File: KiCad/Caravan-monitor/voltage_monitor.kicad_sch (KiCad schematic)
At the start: 2 parts, among them IC3 INA500CIDBVR

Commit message: Schematics done
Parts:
- C12: footprint Capacitor_SMD:C_0805_2012Metric_Pad1.18x1.45mm_HandSolder -> Capacitor_SMD:C_0402_1005Metric_Pad0.74x0.62mm_HandSolder
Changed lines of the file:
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@@
 			)
 		)
-		(property "Footprint" "Capacitor_SMD:C_0805_2012Metric_Pad1.18x1.45mm_HandSolder"
+		(property "Footprint" "Capacitor_SMD:C_0402_1005Metric_Pad0.74x0.62mm_HandSolder"
 			(at 157.1752 83.82 0)
 			(effects

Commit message: PCB Designed
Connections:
- net 5V renamed Vin
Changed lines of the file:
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@@
 		)
 	)
-	(hierarchical_label "5V"
+	(hierarchical_label "Vin"
 		(shape input)
 		(at 149.86 71.12 90)

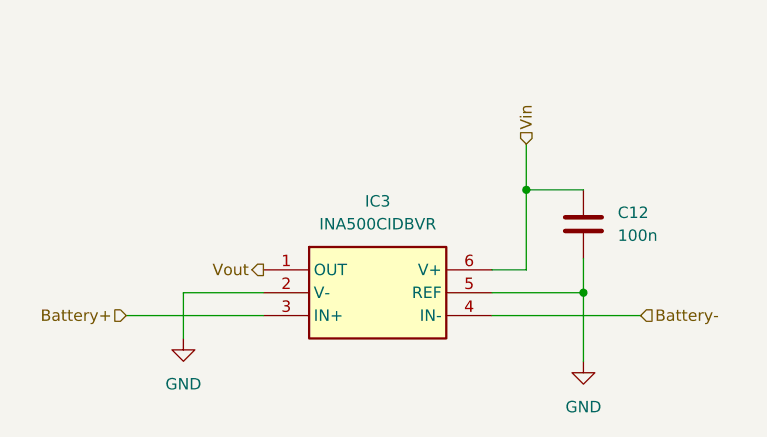
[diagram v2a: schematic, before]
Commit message: Schematic updates
Parts changed for JLCPCB assembly compatibility
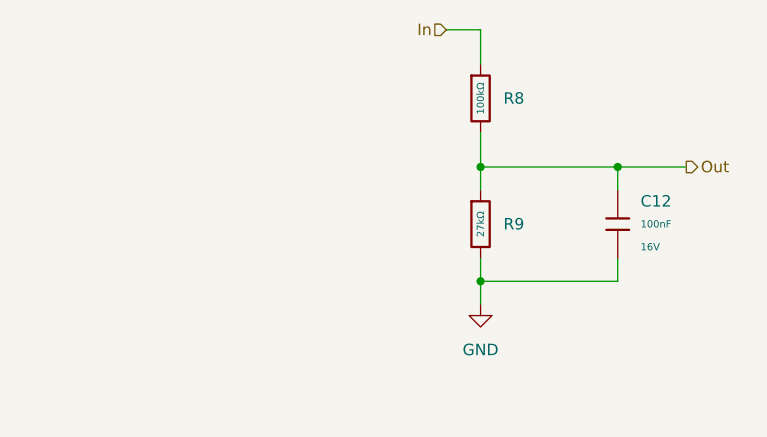
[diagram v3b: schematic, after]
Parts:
- removed C12: 100n, Capacitor_SMD:C_0402_1005Metric_Pad0.74x0.62mm_HandSolder, symbol Device:C
- removed IC3: INA500CIDBVR, SamacSys_Parts:SOT95P280X145-6N, symbol SamacSys_Parts:INA500CIDBVR
- added C12: 100nF, PCM_JLCPCB:C_0402, symbol PCM_JLCPCB-Capacitors:0402,100nF
- added R8: 100kΩ, PCM_JLCPCB:R_0402, symbol PCM_JLCPCB-Resistors:0402,100kΩ
- added R9: 27kΩ, PCM_JLCPCB:R_0402, symbol PCM_JLCPCB-Resistors:0402,27kΩ
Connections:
- net GND: now also C12.2, R9.2
- new net In: R8.1
- new net Out: C12.1, R8.2, R9.1
